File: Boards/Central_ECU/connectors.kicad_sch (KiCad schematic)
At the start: 44 parts, among them J10 Solenoid NANOFIT, J11 DB9 Microfit, J12 RS422 JST, J13 USB_B_Micro, J14 SWD JST PH, J15 UART JST, J2 Extras JST, J3 MICROFIT, J4 Siren MICROFIT, J5 I2CB JST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

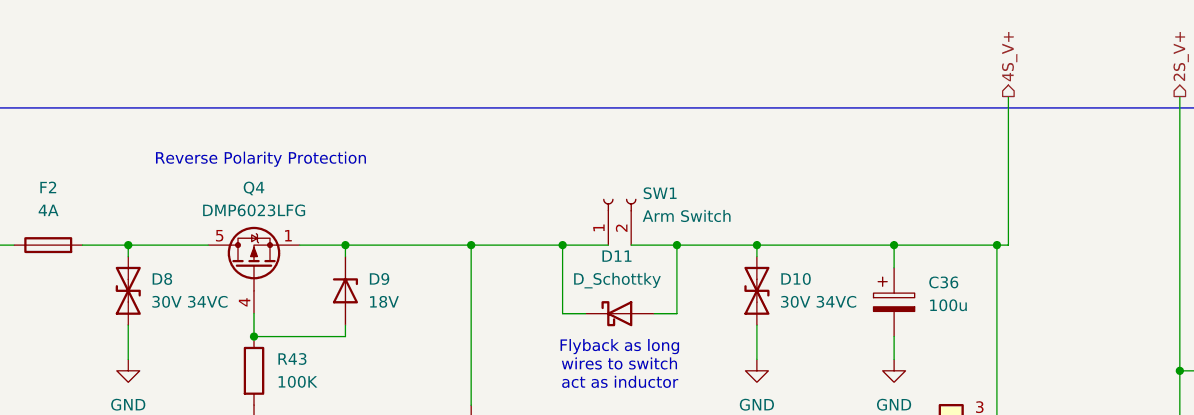
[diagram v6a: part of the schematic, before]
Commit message: Central ECU to order
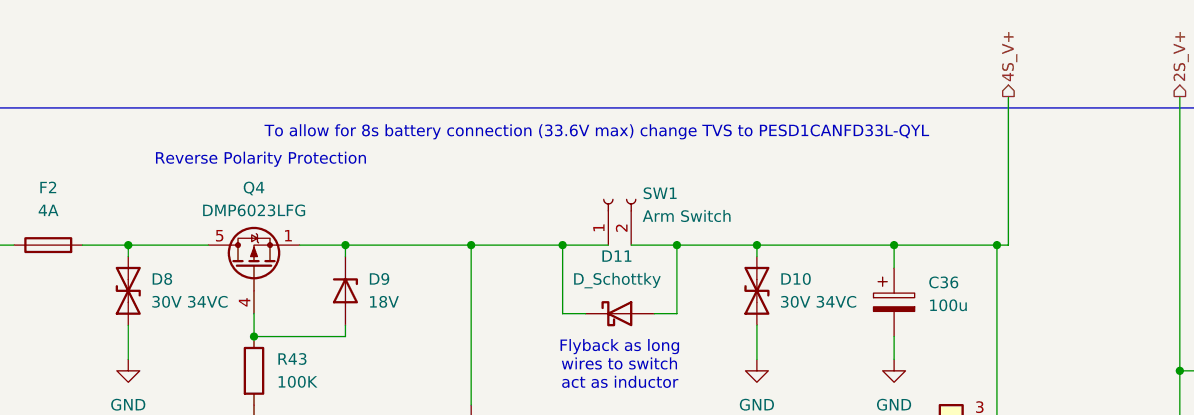
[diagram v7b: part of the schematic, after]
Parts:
- C36, C41: MPN A768KE107M1VLAE036 -> A768KS107M1HLAE030
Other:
- note added: "To allow for 8s battery connection (33.6V max) change TVS to PESD1CANFD33L-QYL"
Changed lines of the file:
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@@
 		)
 	)
+	(text "To allow for 8s battery connection (33.6V max) change TVS to PESD1CANFD33L-QYL"
+		(exclude_from_sim no)
+		(at 143.51 37.084 0)
+		(effects
+			(font
+				(size 1.27 1.27)
+			)
+		)
+	)
 	(text "USB"
 		(exclude_from_sim no)
@@
 			)
 		)
-		(property "Datasheet" "https://content.kemet.com/datasheets/KEM_A4088_A768.pdf"
+		(property "Datasheet" "https://search.kemet.com/download/datasheet/A768KS107M1HLAE030"
 			(at 176.53 55.88 0)
 			(effects
@@
 			)
 		)
-		(property "MPN" "A768KE107M1VLAE036"
+		(property "MPN" "A768KS107M1HLAE030"
 			(at 176.53 55.88 0)
 			(effects
@@
 			)
 		)
-		(property "Datasheet" "https://content.kemet.com/datasheets/KEM_A4088_A768.pdf"
+		(property "Datasheet" "https://search.kemet.com/download/datasheet/A768KS107M1HLAE030"
 			(at 172.72 97.79 0)
 			(effects
@@
 			)
 		)
-		(property "MPN" "A768KE107M1VLAE036"
+		(property "MPN" "A768KS107M1HLAE030"
 			(at 172.72 97.79 0)
 			(effects

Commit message: Cleaning out code for firmware
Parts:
- J8: MPN B4B-PH-K-S -> B4B-EH-A
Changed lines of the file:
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@@
 			)
 		)
-		(property "MPN" "B4B-PH-K-S"
+		(property "MPN" "B4B-EH-A"
 			(at 363.22 167.64 90)
 			(effects
